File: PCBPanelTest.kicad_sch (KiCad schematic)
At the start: 3 parts

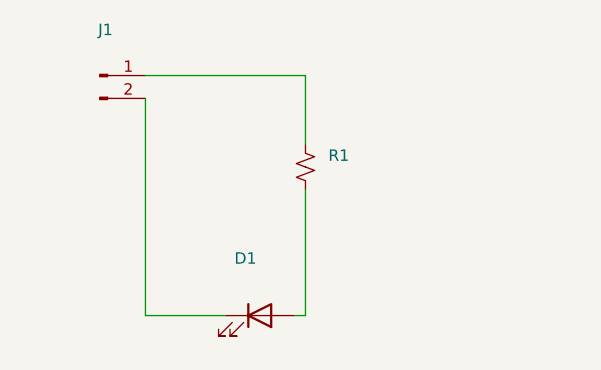
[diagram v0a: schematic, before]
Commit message: add kibot workflow
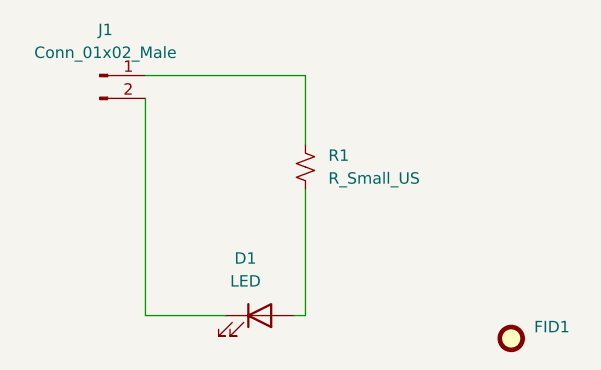
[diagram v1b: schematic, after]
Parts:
- added FID1: (no value), symbol Mechanical:Fiducial
- D1: value (none) -> LED; footprint (none) -> LED_SMD:LED_0805_2012Metric
- J1: value (none) -> Conn_01x02_Male; footprint (none) -> Connector_PinHeader_1.00mm:PinHeader_1x02_P1.00mm_Vertical
- R1: value (none) -> R_Small_US; footprint (none) -> Resistor_SMD:R_0805_2012Metric
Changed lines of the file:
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@@
       (effects (font (size 1.27 1.27)) (justify left))
     )
-    (property "Value" "" (id 1) (at 125.73 58.4199 0)
+    (property "Value" "R_Small_US" (id 1) (at 125.73 58.4199 0)
       (effects (font (size 1.27 1.27)) (justify left))
     )
-    (property "Footprint" "" (id 2) (at 123.19 57.15 0)
+    (property "Footprint" "Resistor_SMD:R_0805_2012Metric" (id 2) (at 123.19 57.15 0)
       (effects (font (size 1.27 1.27)) hide)
     )
@@
     (pin "2")
   )
+  (symbol (lib_id "Mechanical:Fiducial") (at 146.05 76.2 0) (unit 1)
+    (in_bom yes) (on_board yes) (fields_autoplaced)
+    (property "Reference" "FID1" (id 0) (at 148.59 74.9299 0)
+      (effects (font (size 1.27 1.27)) (justify left))
+    )
+    (property "Value" "" (id 1) (at 148.59 77.4699 0)
+      (effects (font (size 1.27 1.27)) (justify left))
+    )
+    (property "Footprint" "" (id 2) (at 146.05 76.2 0)
+      (effects (font (size 1.27 1.27)) hide)
+    )
+    (property "Datasheet" "~" (id 3) (at 146.05 76.2 0)
+      (effects (font (size 1.27 1.27)) hide)
+    )
+  )
   (symbol (lib_id "Device:LED") (at 118.11 73.66 0) (unit 1)
     (in_bom yes) (on_board yes) (fields_autoplaced)
     (property "Reference" "D1" (id 0) (at 116.5225 67.31 0))
-    (property "Value" "" (id 1) (at 116.5225 69.85 0))
-    (property "Footprint" "" (id 2) (at 118.11 73.66 0)
+    (property "Value" "LED" (id 1) (at 116.5225 69.85 0))
+    (property "Footprint" "LED_SMD:LED_0805_2012Metric" (id 2) (at 118.11 73.66 0)
       (effects (font (size 1.27 1.27)) hide)
     )
@@
     (in_bom yes) (on_board yes) (fields_autoplaced)
     (property "Reference" "J1" (id 0) (at 100.965 41.91 0))
-    (property "Value" "" (id 1) (at 100.965 44.45 0))
-    (property "Footprint" "" (id 2) (at 100.33 46.99 0)
+    (property "Value" "Conn_01x02_Male" (id 1) (at 100.965 44.45 0))
+    (property "Footprint" "Connector_PinHeader_1.00mm:PinHeader_1x02_P1.00mm_Vertical" (id 2) (at 100.33 46.99 0)
       (effects (font (size 1.27 1.27)) hide)
     )
@@
       (reference "D1") (unit 1) (value "LED") (footprint "LED_SMD:LED_0805_2012Metric")
     )
+    (path "/97f5e67e-06f7-48de-b9ac-126696e0afb0"
+      (reference "FID1") (unit 1) (value "Fiducial") (footprint "Fiducial:Fiducial_1mm_Mask2mm")
+    )
     (path "/f7c782b9-cd50-4cac-b805-2d4531f2747b"
